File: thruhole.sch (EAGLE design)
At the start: 12 parts

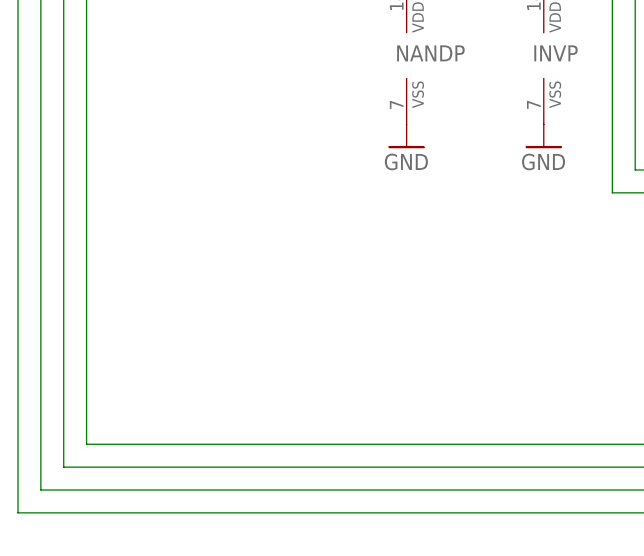
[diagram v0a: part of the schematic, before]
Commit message: WIP: Added 555 timer to thruhole board
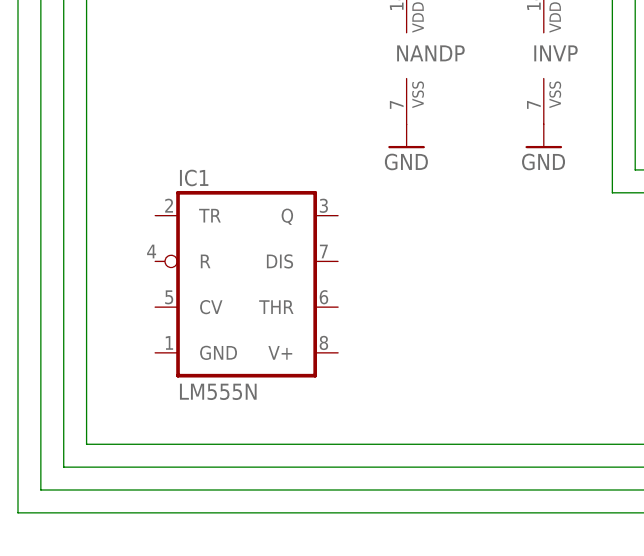
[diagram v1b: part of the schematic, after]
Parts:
- added IC1: LM555N, linear:LM555N
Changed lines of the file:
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@@
 <setting verticaltext="up"/>
 </settings>
-<grid distance="0.1" unitdist="inch" unit="inch" style="lines" multiple="1" display="yes" altdistance="0.01" altunitdist="inch" altunit="inch"/>
+<grid distance="0.1" unitdist="inch" unit="inch" style="lines" multiple="1" display="no" altdistance="0.01" altunitdist="inch" altunit="inch"/>
 <layers>
 <layer number="1" name="Top" color="4" fill="1" visible="no" active="no"/>
@@
 <part name="JP2" library="pinhead" deviceset="PINHD-1X4" device=""/>
 <part name="JP3" library="pinhead" deviceset="PINHD-1X4" device=""/>
+<part name="IC1" library="linear" deviceset="*555" device="N" technology="LM"/>
 </parts>
 <sheets>
@@
 <instance part="JP2" gate="A" x="129.54" y="-15.24"/>
 <instance part="JP3" gate="A" x="104.14" y="-15.24"/>
+<instance part="IC1" gate="A" x="33.02" y="7.62"/>
 </instances>
 <busses>
